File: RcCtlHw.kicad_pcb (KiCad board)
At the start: 2 copper layers, 26.7 x 41.9 mm, 30 parts, among them J1 USB_B_Mini, J2 Program, J3 TFT_LCD, SW1 On/Off, U1 TP4056, U2 ESP-M2, U3 ADS1015, U4 Joystick

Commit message: Ready to etch
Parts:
- added C10: 100n, Capacitor_SMD:C_0805_2012Metric, F.Cu at (174.0, 111.5)
- added C11: 100n, Capacitor_SMD:C_0805_2012Metric, F.Cu at (164.6, 107.7)
- added U5: Left Joystick, TrevM:Joystick, B.Cu at (160.0, 110.2)
- D1: value LED_RCGB -> Chg
- R10: value 10K -> 1K
- U4: value Joystick -> Right Joystick
- V1: value Regulator -> 3V3
- moved R7 38.1 mm to (173.2, 98.2), turned to 90 degrees
- moved J1 36.4 mm to (147.8, 128.5), turned to 180 degrees
- moved R8 28.0 mm to (163.2, 93.3), turned to 0 degrees
- moved J2 23.3 mm to (161.7, 90.4), turned to 270 degrees
- moved U2 22.1 mm to (147.0, 98.0)
- moved R6 20.7 mm to (136.3, 96.0), turned to 90 degrees
- moved SW1 19.0 mm to (160.0, 121.5), turned to 90 degrees
- moved C7 11.0 mm to (129.2, 99.1), turned to 0 degrees
- moved D1 9.26 mm to (122.6, 119.5), turned to 180 degrees
- moved C8 8.20 mm to (134.4, 111.8), turned to 270 degrees
- moved J3 6.38 mm to (137.5, 88.9), turned to 270 degrees
- moved R3 4.55 mm to (121.4, 109.3)
- moved C5 2.71 mm to (118.9, 101.0)
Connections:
- net Net-(C7-Pad1) renamed /RH
- net Net-(C8-Pad1) renamed /RV
- C3 pad 1: Net-(C3-Pad1) -> +3V3
- C4 pad 1: Net-(C3-Pad1) -> +3V3
- SW1 pad 1: Net-(C3-Pad1) -> +BATT
- SW1 pad 2: +3V3 -> Net-(SW1-Pad2)
- U2 pad 1: (no net) -> Net-(C9-Pad1)
- U3 pad 6: Net-(C9-Pad1) -> /LH
- U3 pad 7: (no net) -> /LV
- V1 pad 1: +BATT -> Net-(SW1-Pad2)
- V1 pad 3: Net-(C3-Pad1) -> +3V3
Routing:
- net GND: track 154.4 -> 244.7 mm, vias 3 -> 4
- net /LH: track 0.00 -> 74.6 mm, vias 0 -> 1
- net +3V3: track 154.5 -> 225.0 mm, vias 2 -> 6
- net /LV: track 0.00 -> 68.3 mm, vias 0 -> 1
- net Net-(SW1-Pad2): track 0.00 -> 49.1 mm, vias 0 -> 1
- net /I2C_SCL: track 22.8 -> 52.1 mm
- net Net-(J1-Pad1): track 14.1 -> 38.3 mm
- net Net-(C3-Pad1): track 23.1 -> 0.00 mm, vias 1 -> 0
- net /I2C_SDA: track 19.9 -> 42.0 mm
- net /TFT_RS: track 13.3 -> 33.4 mm
- net Net-(C9-Pad1): track 13.1 -> 29.0 mm, vias 0 -> 1
- net /RX: track 10.5 -> 25.6 mm
- net +BATT: track 85.2 -> 98.1 mm
- net /TX: track 10.4 -> 22.4 mm
- net Net-(D1-Pad3): track 7.05 -> 17.5 mm
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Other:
- board size 26.7 x 41.9 mm -> 67.7 x 41.9 mm
- board text removed: "Ctrl"
- board text removed: "RC"

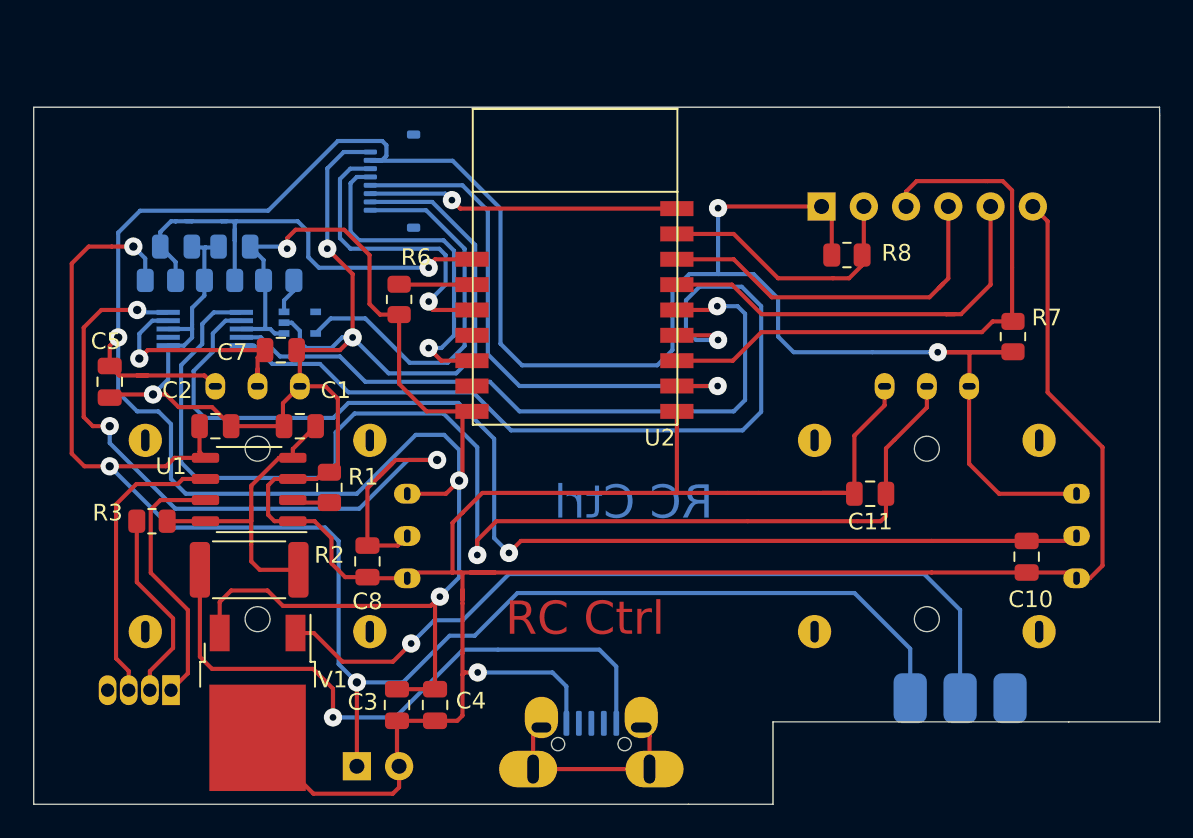
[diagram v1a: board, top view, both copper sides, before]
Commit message: Added fixing holes, ready for making
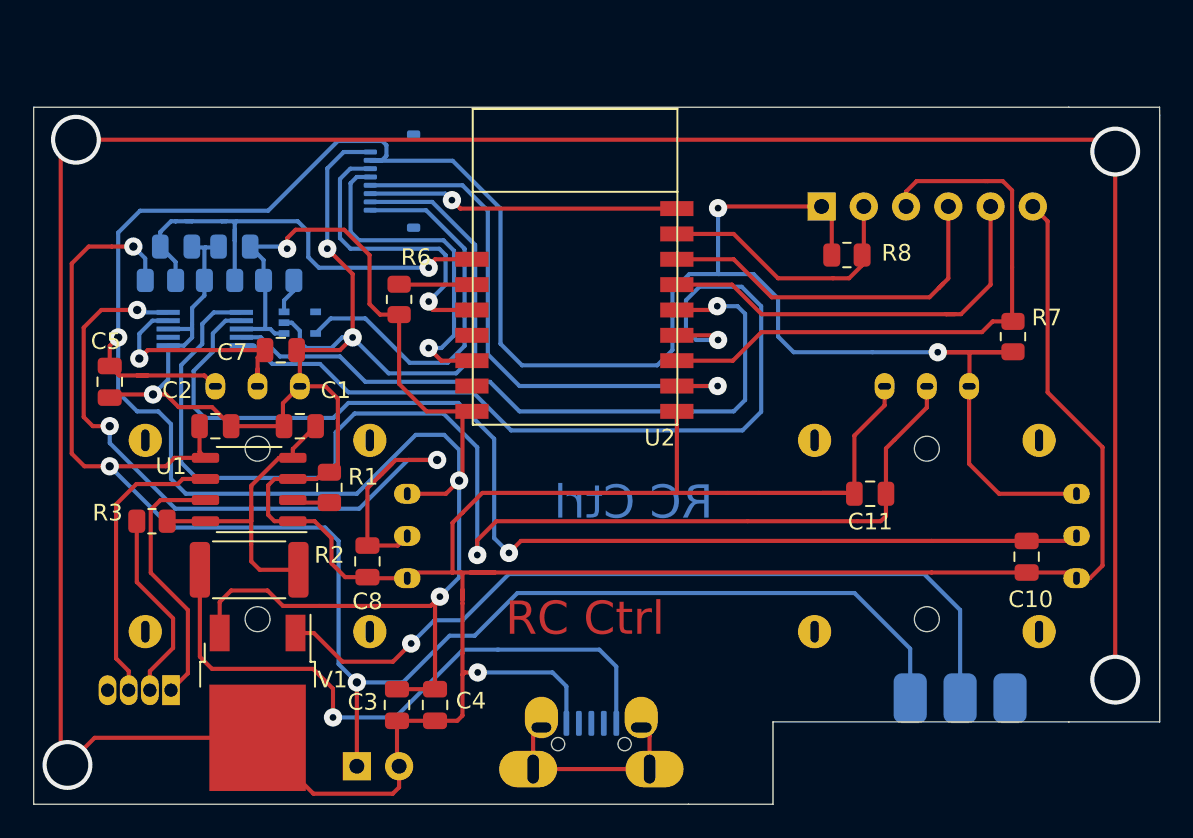
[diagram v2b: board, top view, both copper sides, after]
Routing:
- net GND: track 244.7 -> 389.5 mm, vias 4 -> 8
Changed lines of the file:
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@@
     (thickness 1.6)
     (drawings 16)
-    (tracks 536)
+    (tracks 548)
     (zones 0)
     (modules 33)
@@
     (effects (font (size 2 2) (thickness 0.5)))
   )
+  (via (at 179.324 87.122) (size 3) (drill 2.5) (layers F.Cu B.Cu) (net 1))
+  (via (at 179.324 118.872) (size 3) (drill 2.5) (layers F.Cu B.Cu) (net 1))
+  (via (at 116.84 86.4108) (size 3) (drill 2.5) (layers F.Cu B.Cu) (net 1))
+  (via (at 116.332 124.0028) (size 3) (drill 2.5) (layers F.Cu B.Cu) (net 1))
   (segment (start 132.08 106.4025) (end 131.7225 106.4025) (width 0.25) (layer F.Cu) (net 1) (status 30))
   (segment (start 131.318 106.807) (end 129.879 106.807) (width 0.25) (layer F.Cu) (net 1) (status 20))
@@
   (segment (start 177.8 112.776) (end 178.562 112.014) (width 0.25) (layer F.Cu) (net 1))
   (segment (start 177 112.776) (end 177.8 112.776) (width 0.25) (layer F.Cu) (net 1))
+  (segment (start 117.9658 122.369) (end 116.332 124.0028) (width 0.25) (layer F.Cu) (net 1))
+  (segment (start 127.762 122.369) (end 117.9658 122.369) (width 0.25) (layer F.Cu) (net 1))
+  (segment (start 116.332 124.0028) (end 115.9256 123.5964) (width 0.25) (layer F.Cu) (net 1))
+  (segment (start 115.9256 87.3252) (end 116.84 86.4108) (width 0.25) (layer F.Cu) (net 1))
+  (segment (start 115.9256 123.5964) (end 115.9256 87.3252) (width 0.25) (layer F.Cu) (net 1))
+  (segment (start 178.6128 86.4108) (end 179.324 87.122) (width 0.25) (layer F.Cu) (net 1))
+  (segment (start 116.84 86.4108) (end 178.6128 86.4108) (width 0.25) (layer F.Cu) (net 1))
+  (segment (start 179.324 87.122) (end 179.324 118.872) (width 0.25) (layer F.Cu) (net 1))
   (segment (start 124.629 109.347) (end 127.381 109.347) (width 0.25) (layer F.Cu) (net 2) (status 10))
   (segment (start 127.381 108.458) (end 127.381 109.347) (width 0.25) (layer F.Cu) (net 2))
